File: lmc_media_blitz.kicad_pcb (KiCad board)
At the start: 2 copper layers, 76.2 x 114.3 mm, 79 parts, among them J3 Conn_ARM_JTAG_SWD_10, Q1 BSS138, Q2 BSS138, U1 TPS61222DCK, U10 SK9822, U11 SK9822, U12 SK9822, U13 SK9822, U14 SK9822, U2 TLV77333PDBVR, U3 LPC804M101JDH20, U4 ST25R3918AQW, Y1 27.12MHz

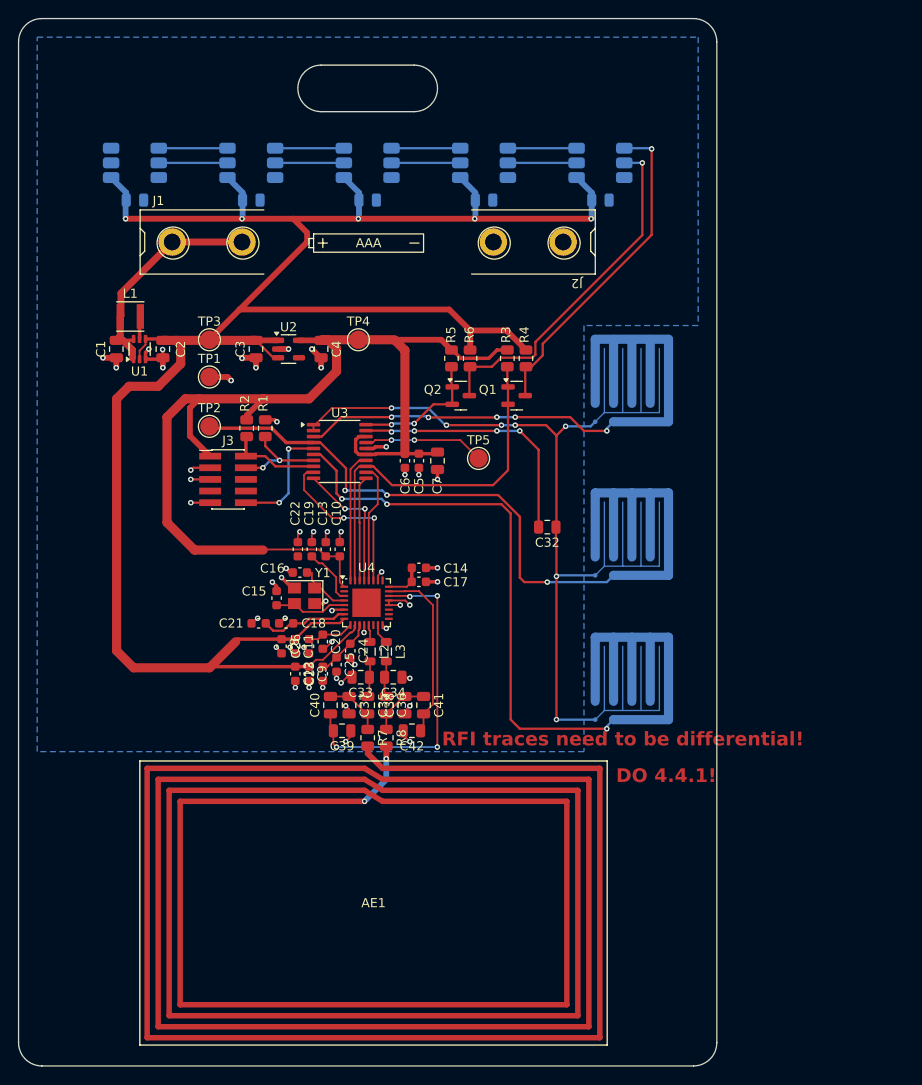
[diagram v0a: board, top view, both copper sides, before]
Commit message: Relayout NFC output
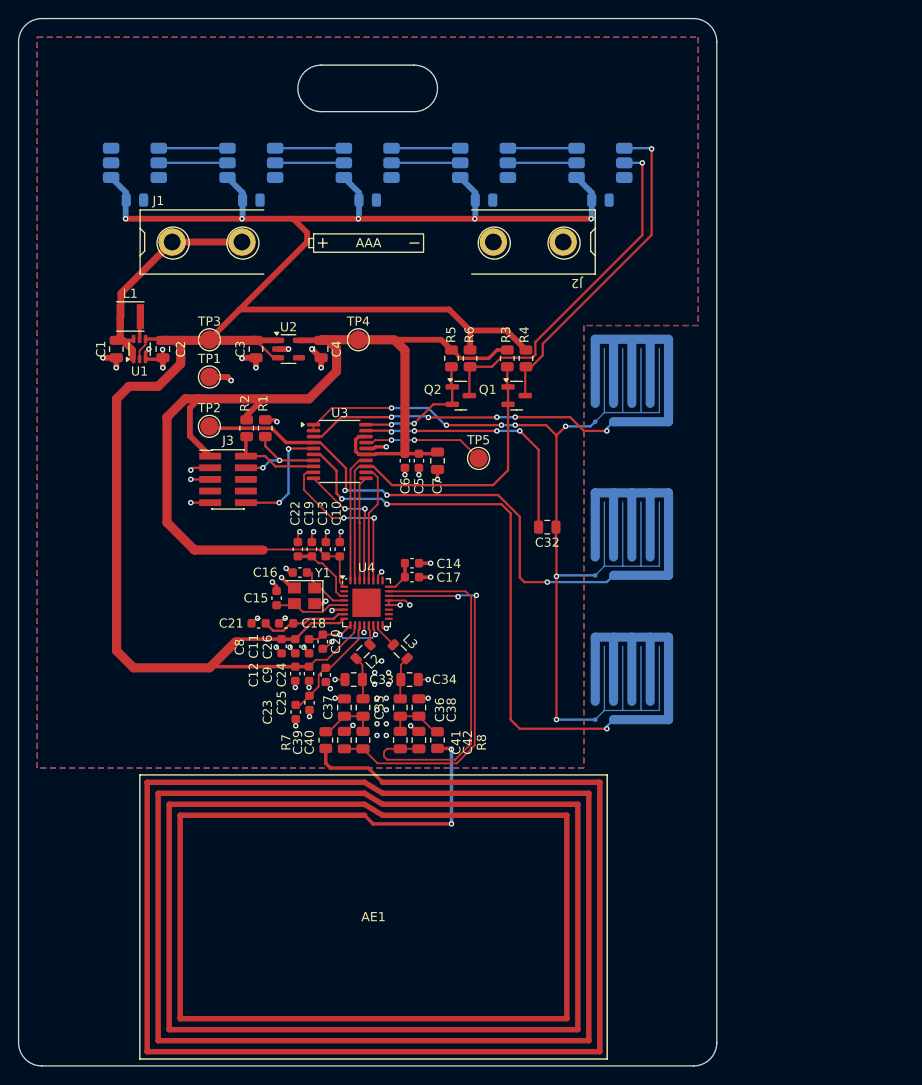
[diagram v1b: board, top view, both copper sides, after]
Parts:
- moved R8 5.59 mm to (160.0, 116.8)
- moved C40 5.21 mm to (151.9, 116.8)
- moved C23 5.11 mm to (144.6, 113.8)
- moved C25 5.11 mm to (146.1, 112.8)
- moved C41 4.58 mm to (156.0, 116.8)
- moved R7 4.58 mm to (147.8, 116.8)
- moved C24 3.75 mm to (147.8, 109.7)
- moved C34 1.80 mm to (157.0, 110.2)
- moved C36 1.55 mm to (156.0, 113.3)
- moved C38 1.55 mm to (158.0, 113.3), turned to -90 degrees
- moved AE1 1.52 mm to (178.0, 151.1)
- moved L3 1.52 mm to (156.0, 107.2), turned to -45 degrees
- moved C42 1.27 mm to (158.0, 116.8), turned to 90 degrees
- moved C39 1.05 mm to (149.9, 116.8), turned to -90 degrees
- moved C14 0.91 mm to (157.2, 97.5)
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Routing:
- net Net-(U4-RFI2): track 19.7 -> 40.5 mm
- net Net-(AE1-Pad2): track 7.01 -> 19.6 mm
- net Net-(AE1-Pad1): track 3.09 -> 8.67 mm
- net Net-(U4-VDD_DR): track 5.16 -> 10.5 mm, vias 0 -> 2
- net Net-(U4-RFI1): track 36.8 -> 41.9 mm, vias 4 -> 2
- net Net-(U4-VDD_AM): track 6.88 -> 11.7 mm
- net GND: track 67.4 -> 65.7 mm
- net Net-(U4-VDD_D): track 6.27 -> 7.79 mm
- net Net-(C33-Pad1): track 3.93 -> 4.71 mm
- net Net-(C34-Pad2): track 3.99 -> 4.71 mm
- net Net-(U4-RFO2): track 2.21 -> 2.84 mm
- net Net-(U4-AGDC): track 4.25 -> 3.71 mm
- net (no net): vias 0 -> 13
- added copper zone on F.Cu, net GND
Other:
- board text removed: "DO 4.4.1!"
- board text removed: "RFI traces need to be differential!"

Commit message: Added more
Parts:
- moved TP5 46.3 mm to (123.4, 64.8)
- moved C10 1.27 mm to (148.6, 95.0), turned to 180 degrees
- moved C22 1.27 mm to (145.5, 95.0), turned to 0 degrees
- moved C13 0.92 mm to (148.6, 96.5), turned to 180 degrees
- moved C19 0.92 mm to (145.5, 96.5), turned to 180 degrees
- moved REF** 0.15 mm to (152.4, 62.5)
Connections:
- TP5 pad 1: Net-(U3-PIO0_7/ADC_1/ACMPV_{REF}) -> +BATT
- U3 pad 17: Net-(U3-PIO0_7/ADC_1/ACMPV_{REF}) -> +BATT
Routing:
- net +BATT: track 26.6 -> 71.0 mm, vias 0 -> 2
- net Net-(U3-PIO0_7/ADC_1/ACMPV_{REF}): track 13.2 -> 0.00 mm, vias 2 -> 0
- net +5V: track 235.4 -> 247.1 mm
- net +3V3: track 119.8 -> 121.0 mm
- net /SPI0_SCKB: track 14.5 -> 15.2 mm
- net Net-(U4-VDD_D): track 7.79 -> 8.45 mm
- net Net-(U4-XTO): track 5.28 -> 5.83 mm
- net GND: track 65.7 -> 66.2 mm, vias 52 -> 75
- net (no net): vias 13 -> 0
